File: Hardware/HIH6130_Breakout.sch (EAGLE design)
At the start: 12 parts, among them U1 HIH6131

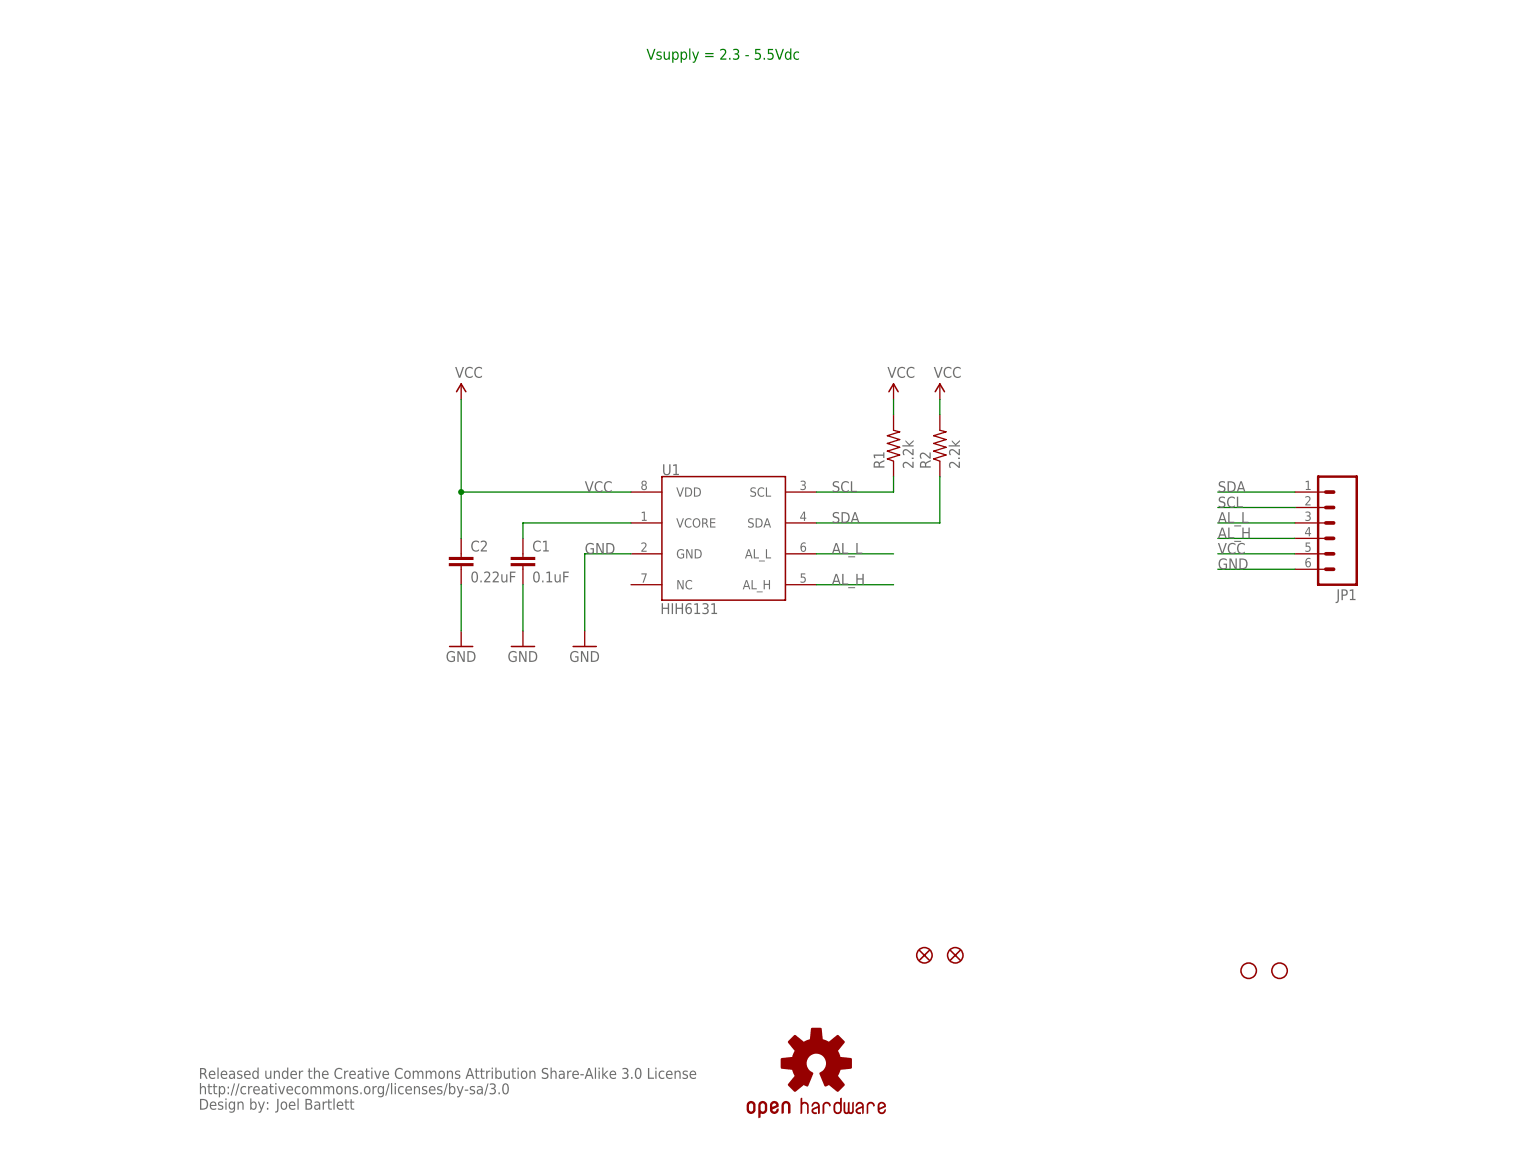
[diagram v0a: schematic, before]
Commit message: 0402-->0603  Schematic Update
Converted all cap/res to 0603 footprint update schematic to "frame
letter"
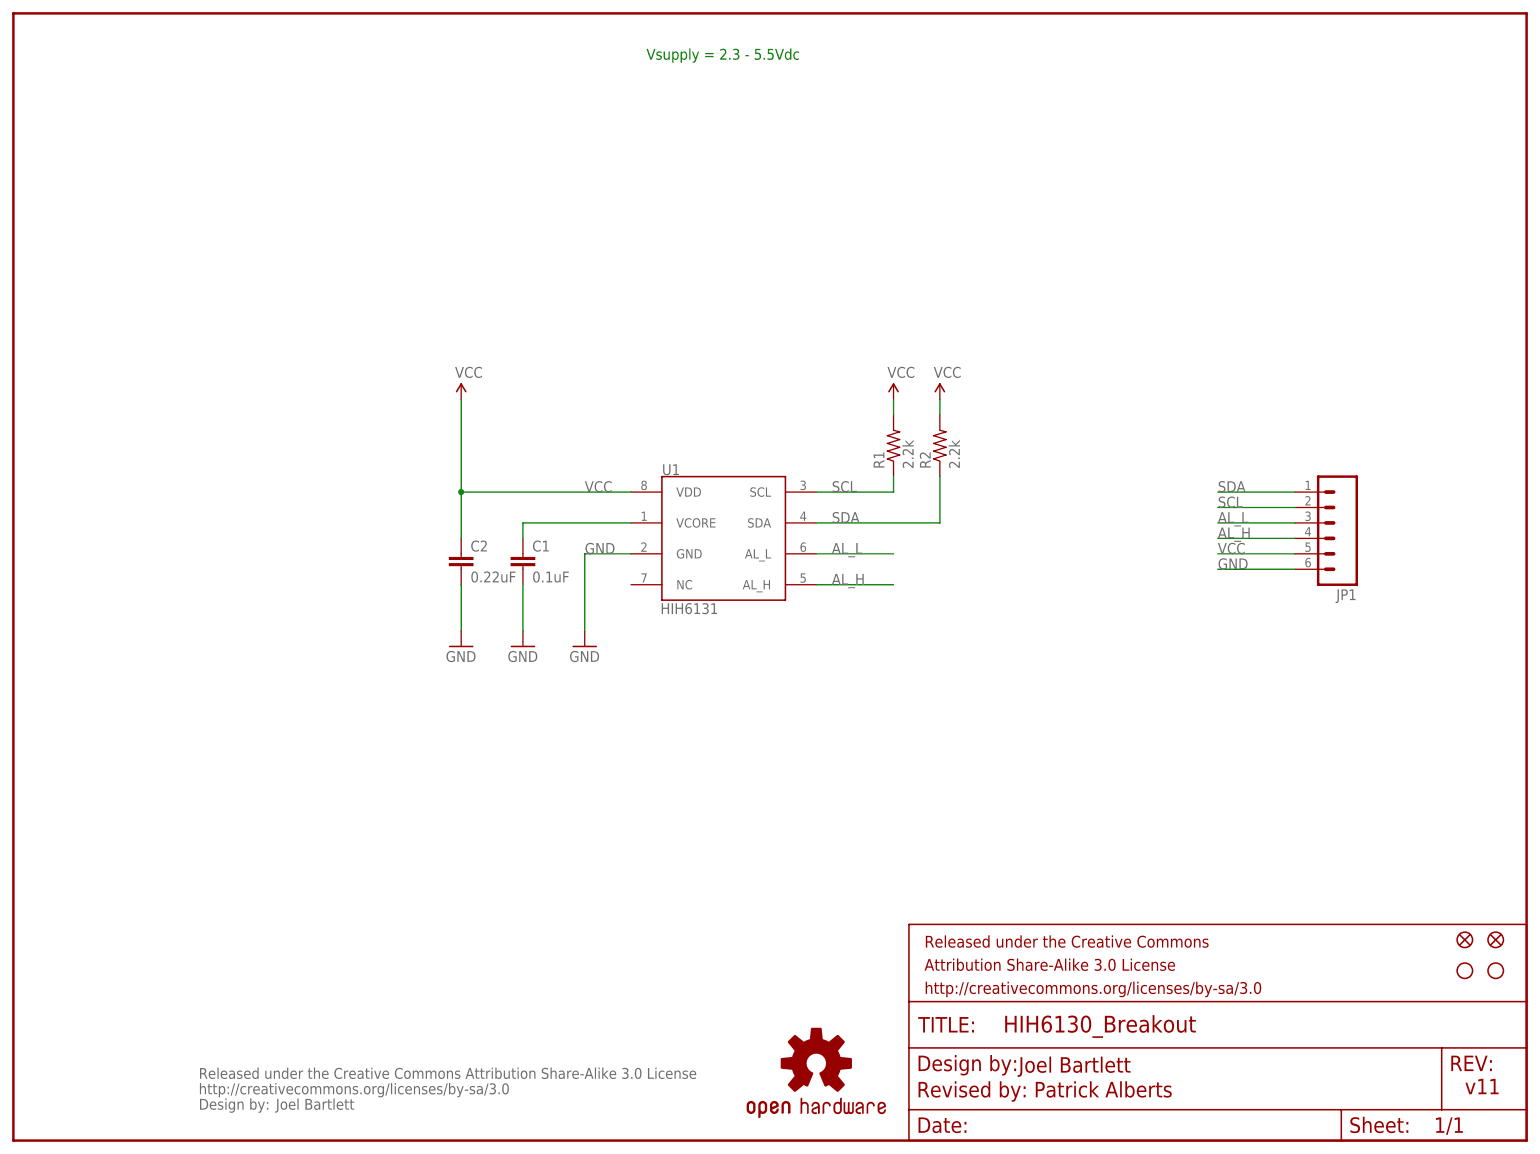
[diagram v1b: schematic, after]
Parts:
- added FRAME1: FRAME-LETTER, SparkFun-Aesthetics:FRAME-LETTER
- C1: device SparkFun:CAP0402-CAP -> SparkFun-Capacitors:0.1UF-25V(+80/-20%)(0603)
- C2: device SparkFun:CAP0402-CAP -> SparkFun-Capacitors:0.22UF-25V-10%(0603)
- R1, R2: device SparkFun:RESISTOR0402-RES -> SparkFun-Resistors:2.2KOHM1/10W1%(0603)
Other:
- note added: "Revised by: Patrick Alberts"
- note added: "v11"
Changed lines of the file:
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@@
 <?xml version="1.0" encoding="utf-8"?>
 <!DOCTYPE eagle SYSTEM "eagle.dtd">
-<eagle version="6.2">
+<eagle version="6.4">
 <drawing>
 <settings>
@@
 <layer number="144" name="Drill_legend" color="7" fill="1" visible="yes" active="yes"/>
 <layer number="151" name="HeatSink" color="7" fill="1" visible="yes" active="yes"/>
+<layer number="199" name="Contour" color="7" fill="1" visible="yes" active="yes"/>
 <layer number="200" name="200bmp" color="1" fill="10" visible="no" active="no"/>
 <layer number="201" name="201bmp" color="2" fill="1" visible="no" active="no"/>
@@
 </classes>
 <parts>
-<part name="FRAME1" library="SparkFun" deviceset="FRAME-LETTER" device=""/>
+<part name="FRAME1" library="SparkFun-Aesthetics" deviceset="FRAME-LETTER" device=""/>
 <part name="JP3" library="SparkFun" deviceset="STAND-OFF" device="TIGHT"/>
 <part name="JP4" library="SparkFun" deviceset="STAND-OFF" device="TIGHT"/>
@@
 <part name="P+1" library="SparkFun" deviceset="VCC" device=""/>
 <part name="GND1" library="SparkFun" deviceset="GND" device=""/>
-<part name="C1" library="SparkFun" deviceset="CAP" device="0402-CAP" value="0.1uF"/>
-<part name="C2" library="SparkFun" deviceset="CAP" device="0402-CAP" value="0.22uF"/>
-<part name="R1" library="SparkFun" deviceset="RESISTOR" device="0402-RES" value="2.2k"/>
-<part name="R2" library="SparkFun" deviceset="RESISTOR" device="0402-RES" value="2.2k"/>
+<part name="C1" library="SparkFun-Capacitors" deviceset="0.1UF-25V(+80/-20%)(0603)" device="" value="0.1uF"/>
+<part name="C2" library="SparkFun-Capacitors" deviceset="0.22UF-25V-10%(0603)" device="" value="0.22uF"/>
+<part name="R1" library="SparkFun-Resistors" deviceset="2.2KOHM1/10W1%(0603)" device="" value="2.2k"/>
+<part name="R2" library="SparkFun-Resistors" deviceset="2.2KOHM1/10W1%(0603)" device="" value="2.2k"/>
 <part name="GND2" library="SparkFun" deviceset="GND" device=""/>
 <part name="GND3" library="SparkFun" deviceset="GND" device=""/>
@@
 <text x="104.14" y="177.8" size="1.778" layer="91">Vsupply = 2.3 - 5.5Vdc</text>
 <text x="43.18" y="5.08" size="1.778" layer="95">Joel Bartlett</text>
+<text x="238.76" y="7.62" size="2.54" layer="94">v11</text>
+<text x="165.354" y="11.176" size="2.54" layer="94">Joel Bartlett</text>
+<text x="148.59" y="7.112" size="2.54" layer="94">Revised by: Patrick Alberts</text>
 </plain>
 <instances>
 <instance part="FRAME1" gate="G$1" x="0" y="0"/>
 <instance part="FRAME1" gate="G$2" x="147.32" y="0"/>
-<instance part="JP3" gate="G$1" x="208.28" y="27.94"/>
-<instance part="JP4" gate="G$1" x="203.2" y="27.94"/>
+<instance part="JP3" gate="G$1" x="243.84" y="27.94"/>
+<instance part="JP4" gate="G$1" x="238.76" y="27.94"/>
 <instance part="U1" gate="G$1" x="116.84" y="99.06"/>
 <instance part="P+1" gate="1" x="73.66" y="121.92"/>
@@
 <instance part="U$2" gate="G$1" x="132.08" y="12.7"/>
 <instance part="U$5" gate="G$1" x="30.48" y="5.08"/>
-<instance part="JP2" gate="G$1" x="149.86" y="30.48"/>
-<instance part="JP5" gate="G$1" x="154.94" y="30.48"/>
+<instance part="JP2" gate="G$1" x="238.76" y="33.02"/>
+<instance part="JP5" gate="G$1" x="243.84" y="33.02"/>
 </instances>
 <busses>

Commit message: SCH Cleanup
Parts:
- removed U$5: CREATIVE_COMMONS, SparkFun:CREATIVE_COMMONS
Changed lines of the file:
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@@
 <part name="JP1" library="SparkFun" deviceset="M06" device="SIP"/>
 <part name="U$2" library="SparkFun" deviceset="OSHW-LOGO" device="S"/>
-<part name="U$5" library="SparkFun" deviceset="CREATIVE_COMMONS" device=""/>
 <part name="JP2" library="SparkFun" deviceset="FIDUCIAL" device="UFIDUCIAL"/>
 <part name="JP5" library="SparkFun" deviceset="FIDUCIAL" device="UFIDUCIAL"/>
@@
 <plain>
 <text x="104.14" y="177.8" size="1.778" layer="91">Vsupply = 2.3 - 5.5Vdc</text>
-<text x="43.18" y="5.08" size="1.778" layer="95">Joel Bartlett</text>
 <text x="238.76" y="7.62" size="2.54" layer="94">v11</text>
 <text x="165.354" y="11.176" size="2.54" layer="94">Joel Bartlett</text>
@@
 <instance part="JP1" gate="G$1" x="215.9" y="101.6" rot="R180"/>
 <instance part="U$2" gate="G$1" x="132.08" y="12.7"/>
-<instance part="U$5" gate="G$1" x="30.48" y="5.08"/>
 <instance part="JP2" gate="G$1" x="238.76" y="33.02"/>
 <instance part="JP5" gate="G$1" x="243.84" y="33.02"/>
@@
 <segment>
 <pinref part="JP1" gate="G$1" pin="6"/>
-<wire x1="210.82" y1="93.98" x2="198.12" y2="93.98" width="0.1524" layer="91"/>
-<label x="198.12" y="93.98" size="1.778" layer="95"/>
+<wire x1="210.82" y1="93.98" x2="208.28" y2="93.98" width="0.1524" layer="91"/>
+<label x="208.28" y="93.98" size="1.27" layer="95" rot="R180" xref="yes"/>
 </segment>
 </net>
@@
 </segment>
 <segment>
-<wire x1="210.82" y1="96.52" x2="198.12" y2="96.52" width="0.1524" layer="91"/>
-<label x="198.12" y="96.52" size="1.778" layer="95"/>
+<wire x1="210.82" y1="96.52" x2="208.28" y2="96.52" width="0.1524" layer="91"/>
 <pinref part="JP1" gate="G$1" pin="5"/>
+<label x="208.28" y="96.52" size="1.27" layer="95" rot="R180" xref="yes"/>
 </segment>
 </net>
@@
 </segment>
 <segment>
-<wire x1="210.82" y1="104.14" x2="198.12" y2="104.14" width="0.1524" layer="91"/>
+<wire x1="210.82" y1="104.14" x2="208.28" y2="104.14" width="0.1524" layer="91"/>
 <pinref part="JP1" gate="G$1" pin="2"/>
-<label x="198.12" y="104.14" size="1.778" layer="95"/>
+<label x="208.28" y="104.14" size="1.27" layer="95" rot="R180" xref="yes"/>
 </segment>
 </net>
@@
 <segment>
 <pinref part="JP1" gate="G$1" pin="1"/>
-<wire x1="210.82" y1="106.68" x2="198.12" y2="106.68" width="0.1524" layer="91"/>
-<label x="198.12" y="106.68" size="1.778" layer="95"/>
+<wire x1="210.82" y1="106.68" x2="208.28" y2="106.68" width="0.1524" layer="91"/>
+<label x="208.28" y="106.68" size="1.27" layer="95" rot="R180" xref="yes"/>
 </segment>
 </net>
@@
 <segment>
 <pinref part="U1" gate="G$1" pin="AL_L"/>
-<wire x1="132.08" y1="96.52" x2="144.78" y2="96.52" width="0.1524" layer="91"/>
-<label x="134.62" y="96.52" size="1.778" layer="95"/>
+<wire x1="132.08" y1="96.52" x2="134.62" y2="96.52" width="0.1524" layer="91"/>
+<label x="134.62" y="96.52" size="1.27" layer="95" xref="yes"/>
 </segment>
 <segment>
-<wire x1="210.82" y1="101.6" x2="198.12" y2="101.6" width="0.1524" layer="91"/>
-<label x="198.12" y="101.6" size="1.778" layer="95"/>
+<wire x1="210.82" y1="101.6" x2="208.28" y2="101.6" width="0.1524" layer="91"/>
 <pinref part="JP1" gate="G$1" pin="3"/>
+<label x="208.28" y="101.6" size="1.27" layer="95" rot="R180" xref="yes"/>
 </segment>
 </net>
@@
 <segment>
 <pinref part="U1" gate="G$1" pin="AL_H"/>
-<wire x1="132.08" y1="91.44" x2="144.78" y2="91.44" width="0.1524" layer="91"/>
-<label x="134.62" y="91.44" size="1.778" layer="95"/>
+<wire x1="132.08" y1="91.44" x2="134.62" y2="91.44" width="0.1524" layer="91"/>
+<label x="134.62" y="91.44" size="1.27" layer="95" xref="yes"/>
 </segment>
 <segment>
-<wire x1="210.82" y1="99.06" x2="198.12" y2="99.06" width="0.1524" layer="91"/>
-<label x="198.12" y="99.06" size="1.778" layer="95"/>
+<wire x1="210.82" y1="99.06" x2="208.28" y2="99.06" width="0.1524" layer="91"/>
 <pinref part="JP1" gate="G$1" pin="4"/>
+<label x="208.28" y="99.06" size="1.27" layer="95" rot="R180" xref="yes"/>
 </segment>
 </net>

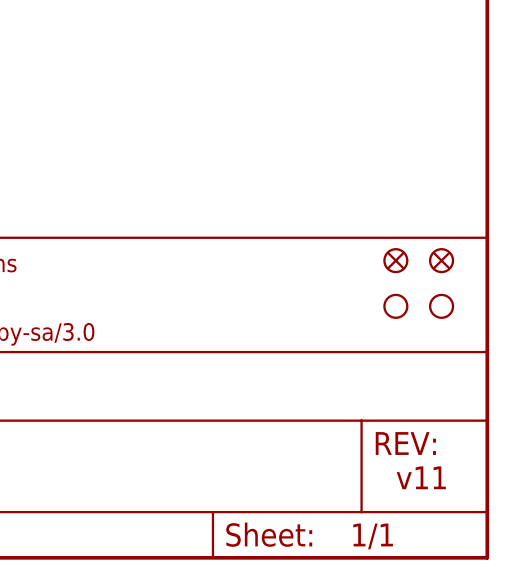
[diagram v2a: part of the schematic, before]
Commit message: added regular fiducials
also deleted older panel
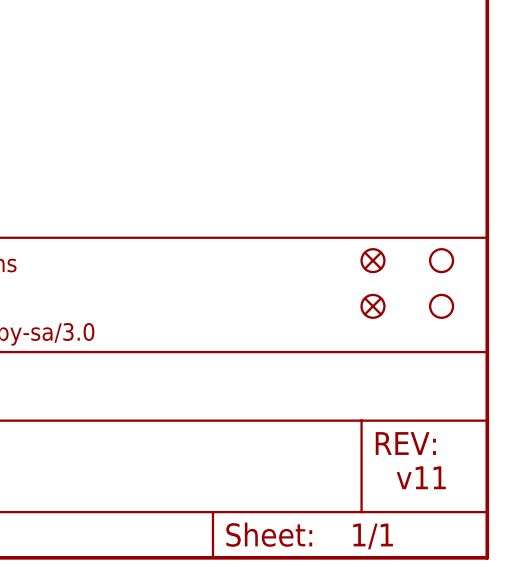
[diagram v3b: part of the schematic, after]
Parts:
- removed JP2, JP5: FIDUCIALUFIDUCIAL, SparkFun:FIDUCIALUFIDUCIAL
- added FID1, FID2: FIDUCIAL1X2, SparkFun-Aesthetics:FIDUCIAL1X2
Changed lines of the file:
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@@
 <?xml version="1.0" encoding="utf-8"?>
 <!DOCTYPE eagle SYSTEM "eagle.dtd">
-<eagle version="6.4">
+<eagle version="6.5.0">
 <drawing>
 <settings>
@@
 <layer number="106" name="bPlate" color="7" fill="1" visible="yes" active="yes"/>
 <layer number="107" name="Crop" color="7" fill="1" visible="yes" active="yes"/>
+<layer number="108" name="tplace-old" color="10" fill="1" visible="no" active="yes"/>
+<layer number="109" name="ref-old" color="11" fill="1" visible="no" active="yes"/>
 <layer number="116" name="Patch_BOT" color="9" fill="4" visible="yes" active="yes"/>
 <layer number="121" name="_tsilk" color="7" fill="1" visible="yes" active="yes"/>
@@
 <part name="JP1" library="SparkFun" deviceset="M06" device="SIP"/>
 <part name="U$2" library="SparkFun" deviceset="OSHW-LOGO" device="S"/>
-<part name="JP2" library="SparkFun" deviceset="FIDUCIAL" device="UFIDUCIAL"/>
-<part name="JP5" library="SparkFun" deviceset="FIDUCIAL" device="UFIDUCIAL"/>
+<part name="FID1" library="SparkFun-Aesthetics" deviceset="FIDUCIAL" device="1X2"/>
+<part name="FID2" library="SparkFun-Aesthetics" deviceset="FIDUCIAL" device="1X2"/>
 </parts>
 <sheets>
@@
 <instance part="FRAME1" gate="G$2" x="147.32" y="0"/>
 <instance part="JP3" gate="G$1" x="243.84" y="27.94"/>
-<instance part="JP4" gate="G$1" x="238.76" y="27.94"/>
+<instance part="JP4" gate="G$1" x="243.84" y="33.02"/>
 <instance part="U1" gate="G$1" x="116.84" y="99.06"/>
 <instance part="P+1" gate="1" x="73.66" y="121.92"/>
@@
 <instance part="JP1" gate="G$1" x="215.9" y="101.6" rot="R180"/>
 <instance part="U$2" gate="G$1" x="132.08" y="12.7"/>
-<instance part="JP2" gate="G$1" x="238.76" y="33.02"/>
-<instance part="JP5" gate="G$1" x="243.84" y="33.02"/>
+<instance part="FID1" gate="G$1" x="236.22" y="33.02"/>
+<instance part="FID2" gate="G$1" x="236.22" y="27.94"/>
 </instances>
 <busses>
